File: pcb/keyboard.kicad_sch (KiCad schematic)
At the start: 23 parts, among them SW1 SW_Push, SW2 SW_Push, SW3 RotaryEncoder_Switch, SW4 SW_Push, SW5 SW_Push, SW6 SW_Push, SW7 SW_Push, SW8 SW_Push, SW9 SW_Push, U1 MODULE-SEEEDUINO-XIAO-RP2040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

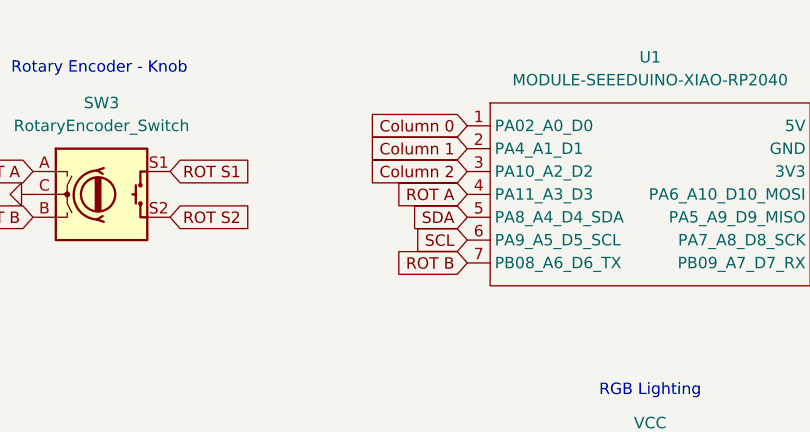
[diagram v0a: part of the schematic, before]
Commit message: swap columns gpio pins for easier pcb routing
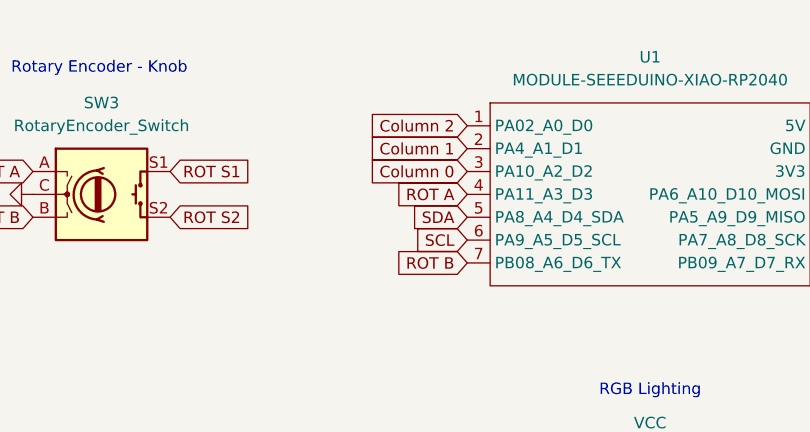
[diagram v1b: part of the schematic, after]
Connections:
- net Column 0: now also U1.3 (PA10_A2_D2); no longer U1.1 (PA02_A0_D0)
- net Column 2: now also U1.1 (PA02_A0_D0); no longer U1.3 (PA10_A2_D2)
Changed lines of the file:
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@@
 	(global_label "Column 0"
 		(shape input)
-		(at 163.83 77.47 180)
+		(at 163.83 82.55 180)
 		(fields_autoplaced yes)
 		(effects
@@
 		)
 		(property "Intersheetrefs" "${INTERSHEET_REFS}"
-			(at 151.5922 77.47 0)
+			(at 155.5835 82.55 0)
 			(hide yes)
 			(show_name no)
@@
 	(global_label "Column 2"
 		(shape input)
-		(at 163.83 82.55 180)
+		(at 163.83 77.47 180)
 		(fields_autoplaced yes)
 		(effects
@@
 		)
 		(property "Intersheetrefs" "${INTERSHEET_REFS}"
-			(at 155.5835 82.55 0)
+			(at 151.5922 77.47 0)
 			(hide yes)
 			(show_name no)
